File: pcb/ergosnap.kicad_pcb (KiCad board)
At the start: 2 copper layers, 133.6 x 132.2 mm, 41 parts, among them J0 Conn_01x05_Female, J1 5PIN, SW1 switch_diode, SW10 switch_diode, SW11 switch_diode, SW12 switch_diode, SW13 switch_diode, SW14 switch_diode, SW15 switch_diode, SW16 switch_diode, SW17 switch_diode, SW18 switch_diode, SW19 switch_diode, SW2 switch_diode, SW20 switch_diode, SW21 switch_diode, SW22 switch_diode, SW23 switch_diode, SW24 switch_diode, SW25 switch_diode, SW26 switch_diode, SW27 switch_diode, SW28 switch_diode, SW3 switch_diode, SW30 switch_diode, SW31 switch_diode, SW32 switch_diode, SW33 switch_diode, SW34 switch_diode, SW35 switch_diode, SW4 switch_diode, SW5 switch_diode, SW6 switch_diode, SW7 switch_diode, SW8 switch_diode, SW9 switch_diode, U3 ProMicro

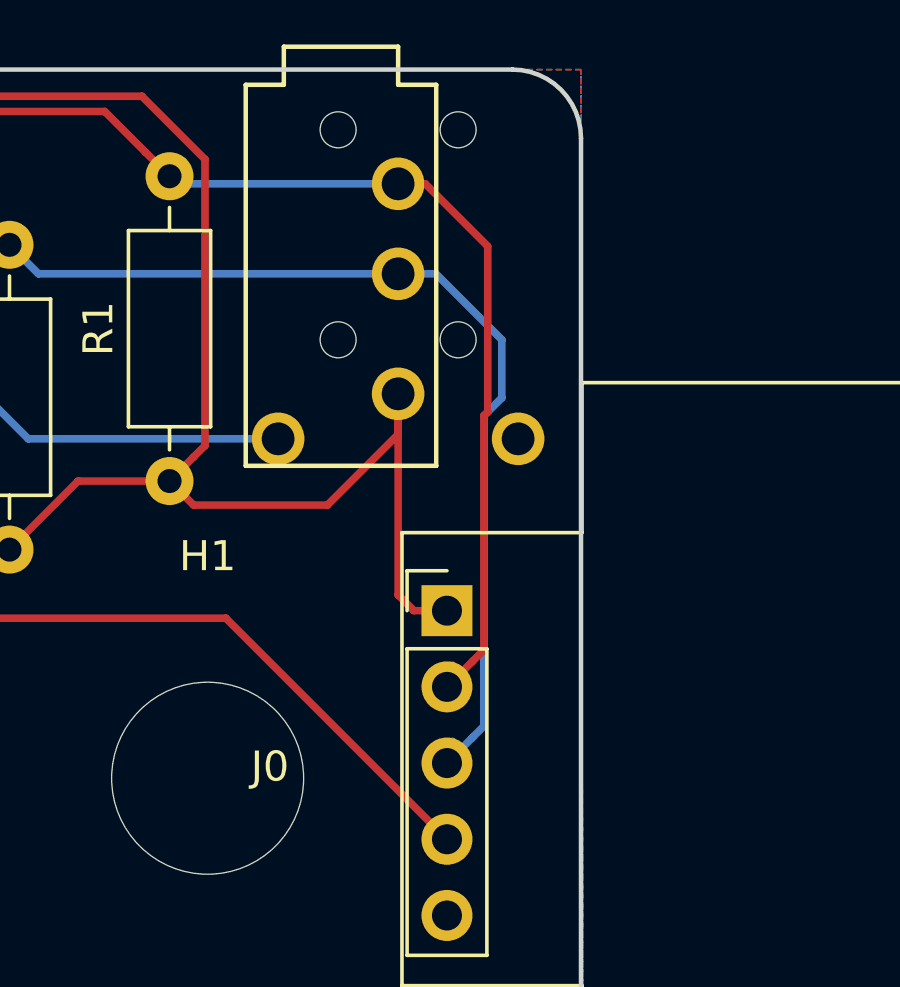
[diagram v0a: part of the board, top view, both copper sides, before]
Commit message: Fiddle with trackball header
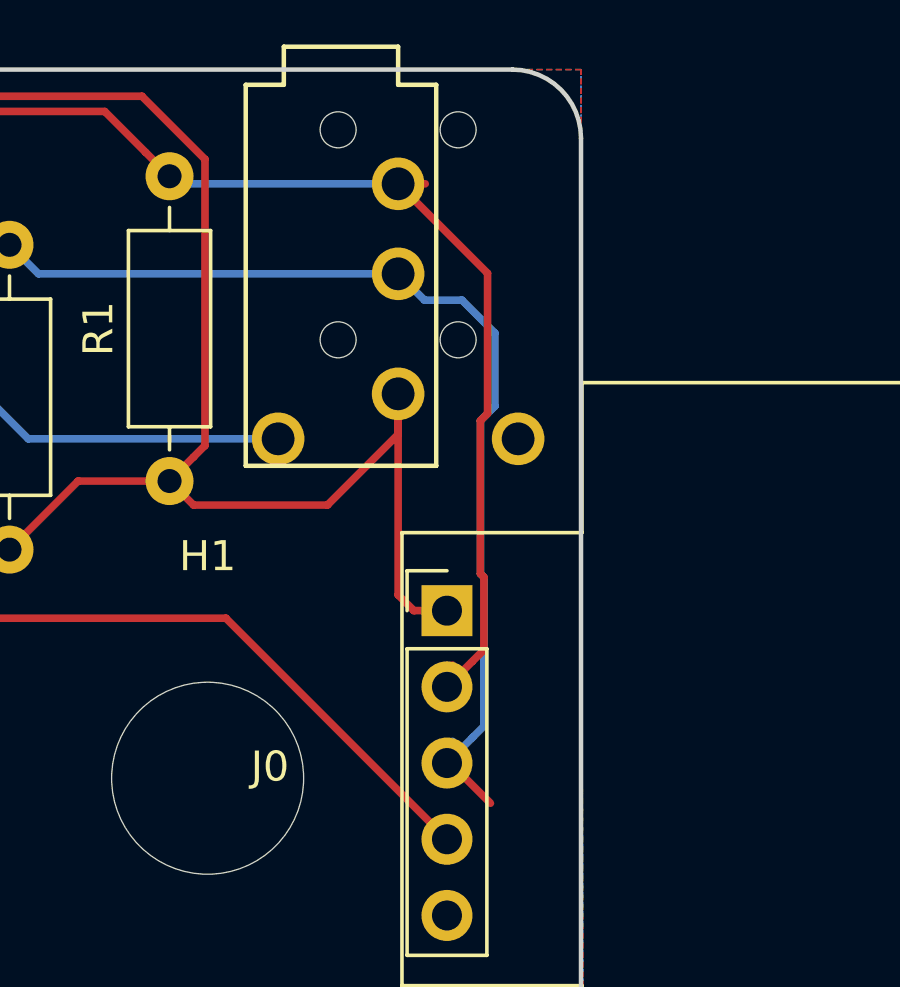
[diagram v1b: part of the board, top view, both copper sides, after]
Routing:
- net /sda: track 73.6 -> 75.5 mm
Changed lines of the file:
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@@
     (thickness 1.6)
     (drawings 22)
-    (tracks 1246)
+    (tracks 1253)
     (zones 0)
     (modules 41)
@@
     (add_net VCC)
   )
+  (module components:pimoroni_trackball (layer F.Cu)
+    (at 207.368 40.896)
+    (descr "Pimoroni I2C trackball breakout")
+    (tags "Through hole pin header THT 1x05 2.54mm single row")
+    (fp_text reference J0 (at -5.9 5.2) (layer F.SilkS)
+      (effects (font (size 1 1) (thickness 0.15)))
+    )
+    (fp_text value Conn_01x05_Female (at 0 12.49) (layer F.Fab)
+      (effects (font (size 1 1) (thickness 0.15)))
+    )
+    (fp_line (start 20.5 17.5) (end 20.5 -7.6) (layer F.SilkS) (width 0.12))
+    (fp_line (start 4.5 -2.6) (end 4.5 -7.6) (layer F.SilkS) (width 0.12))
+    (fp_line (start 4.5 -7.6) (end 20.5 -7.6) (layer F.SilkS) (width 0.12))
+    (fp_line (start -1.5 -2.6) (end 4.5 -2.6) (layer F.SilkS) (width 0.12))
+    (fp_line (start 4.5 17.5) (end 20.5 17.5) (layer F.SilkS) (width 0.12))
+    (fp_line (start 4.5 12.5) (end 4.5 17.5) (layer F.SilkS) (width 0.12))
+    (fp_line (start -1.5 12.5) (end 4.5 12.5) (layer F.SilkS) (width 0.12))
+    (fp_line (start -1.5 -2.6) (end -1.5 12.5) (layer F.SilkS) (width 0.12))
+    (fp_line (start 1.8 -1.8) (end -1.8 -1.8) (layer F.CrtYd) (width 0.05))
+    (fp_line (start 1.8 11.95) (end 1.8 -1.8) (layer F.CrtYd) (width 0.05))
+    (fp_line (start -1.8 11.95) (end 1.8 11.95) (layer F.CrtYd) (width 0.05))
+    (fp_line (start -1.8 -1.8) (end -1.8 11.95) (layer F.CrtYd) (width 0.05))
+    (fp_line (start -1.33 -1.33) (end 0 -1.33) (layer F.SilkS) (width 0.12))
+    (fp_line (start -1.33 0) (end -1.33 -1.33) (layer F.SilkS) (width 0.12))
+    (fp_line (start -1.33 1.27) (end 1.33 1.27) (layer F.SilkS) (width 0.12))
+    (fp_line (start 1.33 1.27) (end 1.33 11.49) (layer F.SilkS) (width 0.12))
+    (fp_line (start -1.33 1.27) (end -1.33 11.49) (layer F.SilkS) (width 0.12))
+    (fp_line (start -1.33 11.49) (end 1.33 11.49) (layer F.SilkS) (width 0.12))
+    (fp_line (start -1.27 -0.635) (end -0.635 -1.27) (layer F.Fab) (width 0.1))
+    (fp_line (start -1.27 11.43) (end -1.27 -0.635) (layer F.Fab) (width 0.1))
+    (fp_line (start 1.27 11.43) (end -1.27 11.43) (layer F.Fab) (width 0.1))
+    (fp_line (start 1.27 -1.27) (end 1.27 11.43) (layer F.Fab) (width 0.1))
+    (fp_line (start -0.635 -1.27) (end 1.27 -1.27) (layer F.Fab) (width 0.1))
+    (pad 5 thru_hole oval (at 0 10.16) (size 1.7 1.7) (drill 1) (layers *.Cu *.Mask)
+      (net 5 GND))
+    (pad 4 thru_hole oval (at 0 7.62) (size 1.7 1.7) (drill 1) (layers *.Cu *.Mask)
+      (net 56 /int0))
+    (pad 3 thru_hole oval (at 0 5.08) (size 1.7 1.7) (drill 1) (layers *.Cu *.Mask)
+      (net 55 /sda))
+    (pad 2 thru_hole oval (at 0 2.54) (size 1.7 1.7) (drill 1) (layers *.Cu *.Mask)
+      (net 7 /scl))
+    (pad 1 thru_hole rect (at 0 0) (size 1.7 1.7) (drill 1) (layers *.Cu *.Mask)
+      (net 6 VCC))
+  )
   (module Resistor_THT:R_Axial_DIN0207_L6.3mm_D2.5mm_P10.16mm_Horizontal (layer F.Cu)
     (at 192.786 38.862 90)
@@
     (pad "" np_thru_hole circle (at 1.5 -2 270) (size 1.2 1.2) (drill 1.2) (layers *.Cu *.Mask F.SilkS))
   )
-  (module components:pimoroni_trackball (layer F.Cu)
-    (at 207.368 40.896)
-    (descr "Pimoroni I2C trackball breakout")
-    (tags "Through hole pin header THT 1x05 2.54mm single row")
-    (fp_text reference J0 (at -5.9 5.2) (layer F.SilkS)
-      (effects (font (size 1 1) (thickness 0.15)))
-    )
-    (fp_text value Conn_01x05_Female (at 0 12.49) (layer F.Fab)
-      (effects (font (size 1 1) (thickness 0.15)))
-    )
-    (fp_line (start 20.5 17.5) (end 20.5 -7.6) (layer F.SilkS) (width 0.12))
-    (fp_line (start 4.5 -2.6) (end 4.5 -7.6) (layer F.SilkS) (width 0.12))
-    (fp_line (start 4.5 -7.6) (end 20.5 -7.6) (layer F.SilkS) (width 0.12))
-    (fp_line (start -1.5 -2.6) (end 4.5 -2.6) (layer F.SilkS) (width 0.12))
-    (fp_line (start 4.5 17.5) (end 20.5 17.5) (layer F.SilkS) (width 0.12))
-    (fp_line (start 4.5 12.5) (end 4.5 17.5) (layer F.SilkS) (width 0.12))
-    (fp_line (start -1.5 12.5) (end 4.5 12.5) (layer F.SilkS) (width 0.12))
-    (fp_line (start -1.5 -2.6) (end -1.5 12.5) (layer F.SilkS) (width 0.12))
-    (fp_line (start 1.8 -1.8) (end -1.8 -1.8) (layer F.CrtYd) (width 0.05))
-    (fp_line (start 1.8 11.95) (end 1.8 -1.8) (layer F.CrtYd) (width 0.05))
-    (fp_line (start -1.8 11.95) (end 1.8 11.95) (layer F.CrtYd) (width 0.05))
-    (fp_line (start -1.8 -1.8) (end -1.8 11.95) (layer F.CrtYd) (width 0.05))
-    (fp_line (start -1.33 -1.33) (end 0 -1.33) (layer F.SilkS) (width 0.12))
-    (fp_line (start -1.33 0) (end -1.33 -1.33) (layer F.SilkS) (width 0.12))
-    (fp_line (start -1.33 1.27) (end 1.33 1.27) (layer F.SilkS) (width 0.12))
-    (fp_line (start 1.33 1.27) (end 1.33 11.49) (layer F.SilkS) (width 0.12))
-    (fp_line (start -1.33 1.27) (end -1.33 11.49) (layer F.SilkS) (width 0.12))
-    (fp_line (start -1.33 11.49) (end 1.33 11.49) (layer F.SilkS) (width 0.12))
-    (fp_line (start -1.27 -0.635) (end -0.635 -1.27) (layer F.Fab) (width 0.1))
-    (fp_line (start -1.27 11.43) (end -1.27 -0.635) (layer F.Fab) (width 0.1))
-    (fp_line (start 1.27 11.43) (end -1.27 11.43) (layer F.Fab) (width 0.1))
-    (fp_line (start 1.27 -1.27) (end 1.27 11.43) (layer F.Fab) (width 0.1))
-    (fp_line (start -0.635 -1.27) (end 1.27 -1.27) (layer F.Fab) (width 0.1))
-    (pad 5 thru_hole oval (at 0 10.16) (size 1.7 1.7) (drill 1) (layers *.Cu *.Mask)
-      (net 5 GND))
-    (pad 4 thru_hole oval (at 0 7.62) (size 1.7 1.7) (drill 1) (layers *.Cu *.Mask)
-      (net 56 /int0))
-    (pad 3 thru_hole oval (at 0 5.08) (size 1.7 1.7) (drill 1) (layers *.Cu *.Mask)
-      (net 55 /sda))
-    (pad 2 thru_hole oval (at 0 2.54) (size 1.7 1.7) (drill 1) (layers *.Cu *.Mask)
-      (net 7 /scl))
-    (pad 1 thru_hole rect (at 0 0) (size 1.7 1.7) (drill 1) (layers *.Cu *.Mask)
-      (net 6 VCC))
-  )
   (module components:cherry_mx_diode_snapout (layer F.Cu)
     (at 200.315 127.2023 60)
@@
   (segment (start 198.372001 26.668) (end 198.120001 26.416) (width 0.254) (layer B.Cu) (net 7))
   (segment (start 205.74 26.668) (end 198.372001 26.668) (width 0.254) (layer B.Cu) (net 7))
+  (segment (start 205.74 26.668) (end 206.644 26.668) (width 0.254) (layer F.Cu) (net 7))
   (segment (start 208.217999 42.586001) (end 207.368 43.436) (width 0.254) (layer F.Cu) (net 7))
   (segment (start 208.599001 42.204999) (end 208.217999 42.586001) (width 0.254) (layer F.Cu) (net 7))
-  (segment (start 208.599001 34.400931) (end 208.599001 42.204999) (width 0.254) (layer F.Cu) (net 7))
-  (segment (start 208.726001 34.273931) (end 208.599001 34.400931) (width 0.254) (layer F.Cu) (net 7))
-  (segment (start 208.726001 28.750001) (end 208.726001 34.273931) (width 0.254) (layer F.Cu) (net 7))
-  (segment (start 206.644 26.668) (end 208.726001 28.750001) (width 0.254) (layer F.Cu) (net 7))
-  (segment (start 205.74 26.668) (end 206.644 26.668) (width 0.254) (layer F.Cu) (net 7))
+  (segment (start 208.599001 39.781301) (end 208.599001 42.204999) (width 0.254) (layer F.Cu) (net 7))
+  (segment (start 208.482699 39.664999) (end 208.599001 39.781301) (width 0.254) (layer F.Cu) (net 7))
+  (segment (start 208.721001 34.326193) (end 208.482699 34.564495) (width 0.254) (layer F.Cu) (net 7))
+  (segment (start 208.721001 29.649001) (end 208.721001 34.326193) (width 0.254) (layer F.Cu) (net 7))
+  (segment (start 208.482699 34.564495) (end 208.482699 39.664999) (width 0.254) (layer F.Cu) (net 7))
+  (segment (start 205.74 26.668) (end 208.721001 29.649001) (width 0.254) (layer F.Cu) (net 7))
   (segment (start 90.7178 60.5155) (end 90.805 60.5155) (width 0.254) (layer B.Cu) (net 8))
   (segment (start 89.535 61.6983) (end 90.7178 60.5155) (width 0.254) (layer B.Cu) (net 8))
@@
   (segment (start 207.556999 45.250999) (end 207.938001 45.632001) (width 0.254) (layer B.Cu) (net 55))
   (segment (start 208.217999 45.126001) (end 207.368 45.976) (width 0.254) (layer B.Cu) (net 55))
-  (segment (start 208.599001 34.400931) (end 208.599001 44.744999) (width 0.254) (layer B.Cu) (net 55))
-  (segment (start 209.198 33.801932) (end 208.599001 34.400931) (width 0.254) (layer B.Cu) (net 55))
-  (segment (start 209.198 31.866718) (end 209.198 33.801932) (width 0.254) (layer B.Cu) (net 55))
   (segment (start 208.599001 44.744999) (end 208.217999 45.126001) (width 0.254) (layer B.Cu) (net 55))
-  (segment (start 206.999282 29.668) (end 209.198 31.866718) (width 0.254) (layer B.Cu) (net 55))
-  (segment (start 205.74 29.668) (end 206.999282 29.668) (width 0.254) (layer B.Cu) (net 55))
+  (segment (start 208.599001 39.781301) (end 208.599001 44.744999) (width 0.254) (layer B.Cu) (net 55))
+  (segment (start 208.482699 39.664999) (end 208.599001 39.781301) (width 0.254) (layer B.Cu) (net 55))
+  (segment (start 208.482699 34.564495) (end 208.482699 39.664999) (width 0.254) (layer B.Cu) (net 55))
+  (segment (start 208.968 34.079194) (end 208.482699 34.564495) (width 0.254) (layer B.Cu) (net 55))
+  (segment (start 208.968 31.644118) (end 208.968 34.079194) (width 0.254) (layer B.Cu) (net 55))
+  (segment (start 207.868181 30.544299) (end 208.968 31.644118) (width 0.254) (layer B.Cu) (net 55))
+  (segment (start 206.616299 30.544299) (end 207.868181 30.544299) (width 0.254) (layer B.Cu) (net 55))
+  (segment (start 205.74 29.668) (end 206.616299 30.544299) (width 0.254) (layer B.Cu) (net 55))
+  (segment (start 207.478 45.976) (end 208.818 47.316) (width 0.254) (layer F.Cu) (net 55))
+  (segment (start 207.368 45.976) (end 207.478 45.976) (width 0.254) (layer F.Cu) (net 55))
   (segment (start 185.42 39.878) (end 186.69 41.148) (width 0.254) (layer F.Cu) (net 56))
   (segment (start 185.42 27.178) (end 185.42 39.878) (width 0.254) (layer F.Cu) (net 56))
